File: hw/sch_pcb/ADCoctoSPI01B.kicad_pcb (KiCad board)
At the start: 2 copper layers, 70.6 x 70.6 mm, 79 parts, among them J1 +5V, J10 HEADER_1x02, J11 HEADER_2x04, J2 SATA7-67491-1030, J3 SATA7-67491-1030, J4 SATA7-67491-1030, J5 SATA7-67491-1030, J6 SAS_mini_1888174, J7 SATA7-67491-1030, J8 HEADER_1x02, J9 HEADER_1x02, M1 HOLE, M2 HOLE, M3 HOLE, M4 HOLE, U1 AFE5801, U2 LM1117MP-1,8/NO, U3 LM1117MP-3,3/NO

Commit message: Edit PCB
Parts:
- C10, C11, C12, C13, C14, C15, C16, C17, C18, C19, C2, C20, C21, C22, C23, C24, C25, C26, C27, C28, C29, C3, C33, C34, C35, C36, C37, C38, C39, C4, C5, C6, C7, C8, C9: footprint Mlab_C:SMD-0603_narrow -> Capacitor_SMD:C_0603_1608Metric
- C30, C31: footprint Mlab_R:SMD-0805 -> Capacitor_SMD:C_0805_2012Metric
- R1, R10, R11, R12, R13, R14, R15, R16, R17, R2, R20, R21, R3, R4, R5, R6, R7, R8, R9: footprint Mlab_R:SMD-0603 -> Resistor_SMD:R_0603_1608Metric
- U2, U3: footprint TO_SOT_Packages_SMD:SOT-223-3_TabPin2 -> Package_TO_SOT_SMD:SOT-223-3_TabPin2
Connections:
- J6 pad A10: (no net) -> unconnected-(J6-PadA10)
- J6 pad A11: (no net) -> unconnected-(J6-PadA11)
- J6 pad B10: (no net) -> unconnected-(J6-PadB10)
- J6 pad B11: (no net) -> unconnected-(J6-PadB11)
- J7 pad 5: (no net) -> unconnected-(J7-Pad5)
- J7 pad 6: (no net) -> unconnected-(J7-Pad6)
- U1 pad 26: (no net) -> unconnected-(U1-Pad26)
- U1 pad 27: (no net) -> unconnected-(U1-Pad27)
- U1 pad 60: (no net) -> unconnected-(U1-Pad60)

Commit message: Edit footprints + 3d models
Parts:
- C1: footprint Capacitors_SMD:C_1210_HandSoldering -> Capacitor_SMD:C_1210_3225Metric_Pad1.33x2.70mm_HandSolder
- D1: footprint Diodes_SMD:D_SMA -> Diode_SMD:D_SMA
- L2, L3, L6: footprint Mlab_R:SMD-0805 -> Inductor_SMD:L_0805_2012Metric_Pad1.15x1.40mm_HandSolder
- M1, M2, M3, M4: footprint VIAS:MountingHole_3mm -> Mlab_Mechanical:MountingHole_3mm

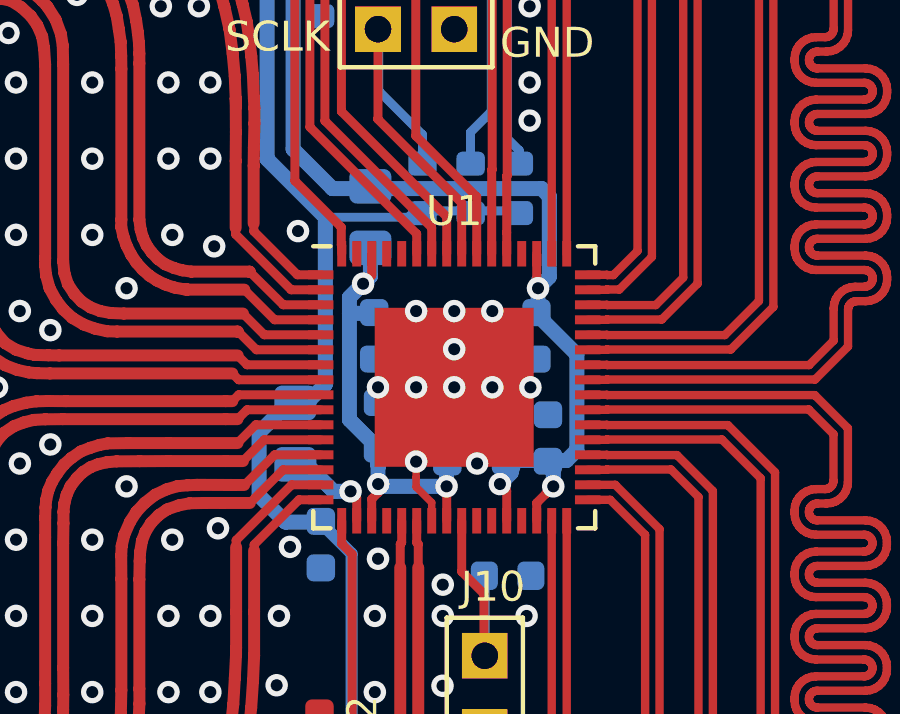
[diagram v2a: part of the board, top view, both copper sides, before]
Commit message: Edit footprint AFE5801
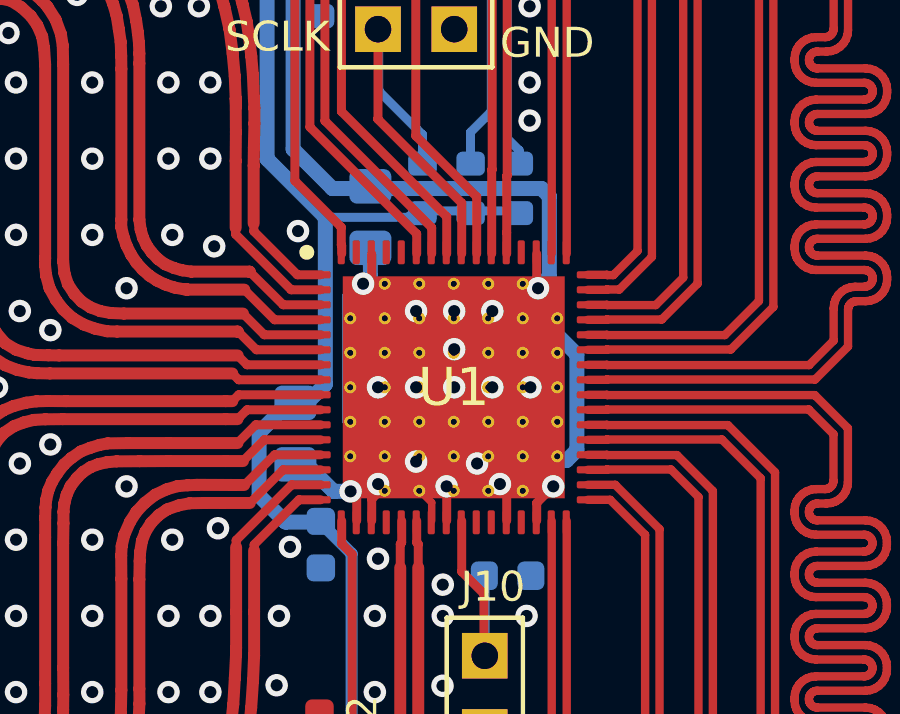
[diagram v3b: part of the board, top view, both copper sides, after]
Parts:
- U1: footprint Mlab_IO:QFN-64-1EP_9x9mm_Pitch0.5mm -> Mlab_IO:VQFN-64_9.15x9.15mm_EP_7.5x7.5mm
- moved U1 3.66 mm to (90.5, 98.7)

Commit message: Edit bom
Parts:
- C1: value 100uF/10V -> 100uF/6V3
- C25: value 100n -> 100nF
- R10, R20: value 127 -> 130
- R11, R21: value 83 -> 82
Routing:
- net GND: track 24.6 -> 104.0 mm, vias 244 -> 251
- net DVDD: track 59.2 -> 0.00 mm, vias 3 -> 0
- net AVDD: track 16.8 -> 0.00 mm, vias 3 -> 0
- net AVDD3V3: track 3.34 -> 0.00 mm, vias 1 -> 0

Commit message: uprava layoutu
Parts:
- moved C20 8.46 mm to (98.4, 100.9), turned to 180 degrees
- moved C21 8.36 mm to (98.4, 99.4), turned to 180 degrees
- moved C19 8.08 mm to (98.4, 97.8), turned to 180 degrees
- moved C36 6.70 mm to (87.4, 100.2), turned to 180 degrees
- moved C39 4.00 mm to (91.2, 110.2), turned to 0 degrees
- moved C35 3.88 mm to (97.5, 105.7), turned to 180 degrees
- moved C34 3.46 mm to (97.5, 102.7), turned to 180 degrees
- moved C33 1.88 mm to (97.5, 104.2), turned to 180 degrees
- moved L3 1.74 mm to (89.7, 94.2), turned to 90 degrees
- moved R14 0.31 mm to (88.4, 88.7)
- moved R13 0.28 mm to (88.4, 85.7)
- moved C27 0.27 mm to (106.3, 69.0)
- moved R15 0.25 mm to (91.4, 95.0)
- moved C31 0.23 mm to (90.3, 74.3)
- moved C28 0.22 mm to (92.2, 74.0)
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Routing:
- net GND: track 104.0 -> 2.94 mm, vias 251 -> 247
- net DVDD: track 0.00 -> 84.6 mm, vias 0 -> 5
- net AVDD: track 0.00 -> 61.2 mm, vias 0 -> 3
- net AVDD3V3: track 0.00 -> 8.15 mm, vias 0 -> 1
- net Net-(C22-Pad2): track 11.5 -> 13.5 mm, vias 0 -> 1
- net Net-(C39-Pad2): track 7.52 -> 6.20 mm
- net Net-(J11-Pad4): track 23.7 -> 24.9 mm
- net VCC: track 25.5 -> 24.6 mm
- net DVDD3V3: track 97.3 -> 96.6 mm
- net unconnected-(J7-Pad6): track 0.56 -> 0.00 mm
- net (no net): vias 1 -> 0

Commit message: uprava layoutu
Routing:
- net GND: track 2.94 -> 9.73 mm
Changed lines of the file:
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@@
   (segment (start 84.82838 116.80952) (end 85.04682 116.32184) (width 0.4) (layer "F.Cu") (net 32))
   (segment (start 79.89316 121.4501) (end 79.89824 121.1707) (width 0.4) (layer "F.Cu") (net 32))
+  (segment (start 90.4448 106.1) (end 90.4448 105.1) (width 0.3) (layer "F.Cu") (net 33))
+  (segment (start 89.4448 97.1) (end 89.4448 97.7448) (width 0.3) (layer "F.Cu") (net 33))
   (segment (start 91.44 104.922002) (end 91.44 104.60732) (width 0.25) (layer "F.Cu") (net 33))
+  (segment (start 90.2 97.9) (end 90.4448 97.6552) (width 0.3) (layer "F.Cu") (net 33))
   (segment (start 112.48028 106.13028) (end 112.522 106.172) (width 0.3) (layer "F.Cu") (net 33))
   (segment (start 114.38028 97.07472) (end 114.427 97.028) (width 0.3) (layer "F.Cu") (net 33))
+  (segment (start 94.9448 106.1) (end 94.9448 105.1) (width 0.3) (layer "F.Cu") (net 33))
+  (segment (start 90.4448 97.6552) (end 90.4448 97.1) (width 0.3) (layer "F.Cu") (net 33))
+  (segment (start 89.6 97.9) (end 90.2 97.9) (width 0.3) (layer "F.Cu") (net 33))
   (segment (start 91.44 104.60732) (end 91.44 104.07699) (width 0.25) (layer "F.Cu") (net 33))
   (segment (start 112.48028 104.51) (end 112.48028 106.13028) (width 0.3) (layer "F.Cu") (net 33))
+  (segment (start 94.9448 97.1) (end 94.9448 98.1) (width 0.2) (layer "F.Cu") (net 33))
+  (segment (start 94.9448 98.1) (end 94.9948 98.15) (width 0.2) (layer "F.Cu") (net 33))
   (segment (start 111.98028 97.06172) (end 112.014 97.028) (width 0.3) (layer "F.Cu") (net 33))
+  (segment (start 94.9448 105.1) (end 94.9948 105.05) (width 0.3) (layer "F.Cu") (net 33))
+  (segment (start 89.4448 97.7448) (end 89.6 97.9) (width 0.3) (layer "F.Cu") (net 33))
+  (segment (start 90.4448 105.1) (end 90.3948 105.05) (width 0.3) (layer "F.Cu") (net 33))
   (segment (start 90.174093 105.110907) (end 90.174093 104.825002) (width 0.3) (layer "F.Cu") (net 33))
+  (segment (start 91.9448 106.1) (end 91.9448 105.45) (width 0.3) (layer "F.Cu") (net 33))
+  (segment (start 91.9448 105.45) (end 91.5448 105.05) (width 0.3) (layer "F.Cu") (net 33))
   (segment (start 123.18028 97.03772) (end 123.19 97.028) (width 0.3) (layer "F.Cu") (net 33))
   (via (at 75.69032 93.977978) (size 0.75) (drill 0.4) (layers "F.Cu" "B.Cu") (net 33))

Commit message: uprava layoutu
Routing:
- net DVDD: track 84.6 -> 87.9 mm
- net DVDD3V3: track 96.6 -> 99.3 mm
- net AVDD3V3: track 8.15 -> 10.3 mm
- net AVDD: track 61.2 -> 62.9 mm
- net GND: vias 247 -> 248

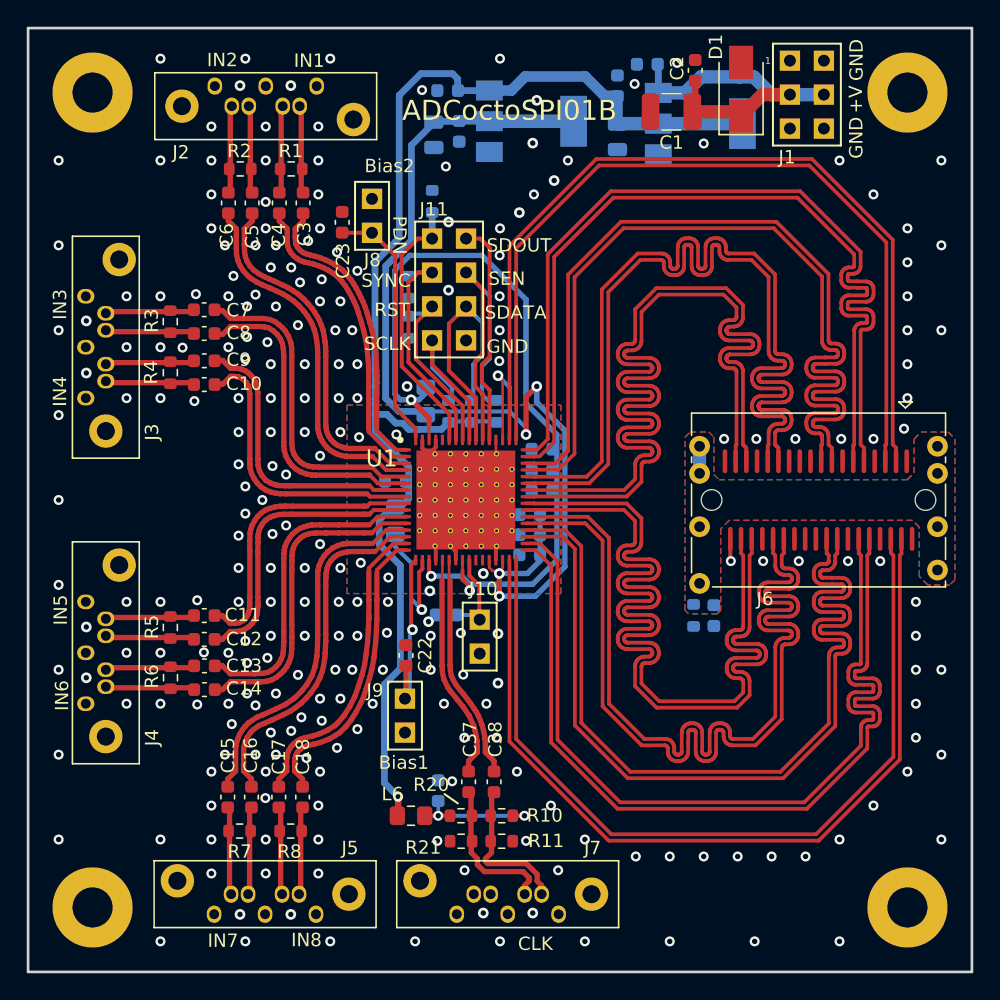
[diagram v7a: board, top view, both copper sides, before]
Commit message: rozdeleni VSSA a VSSD
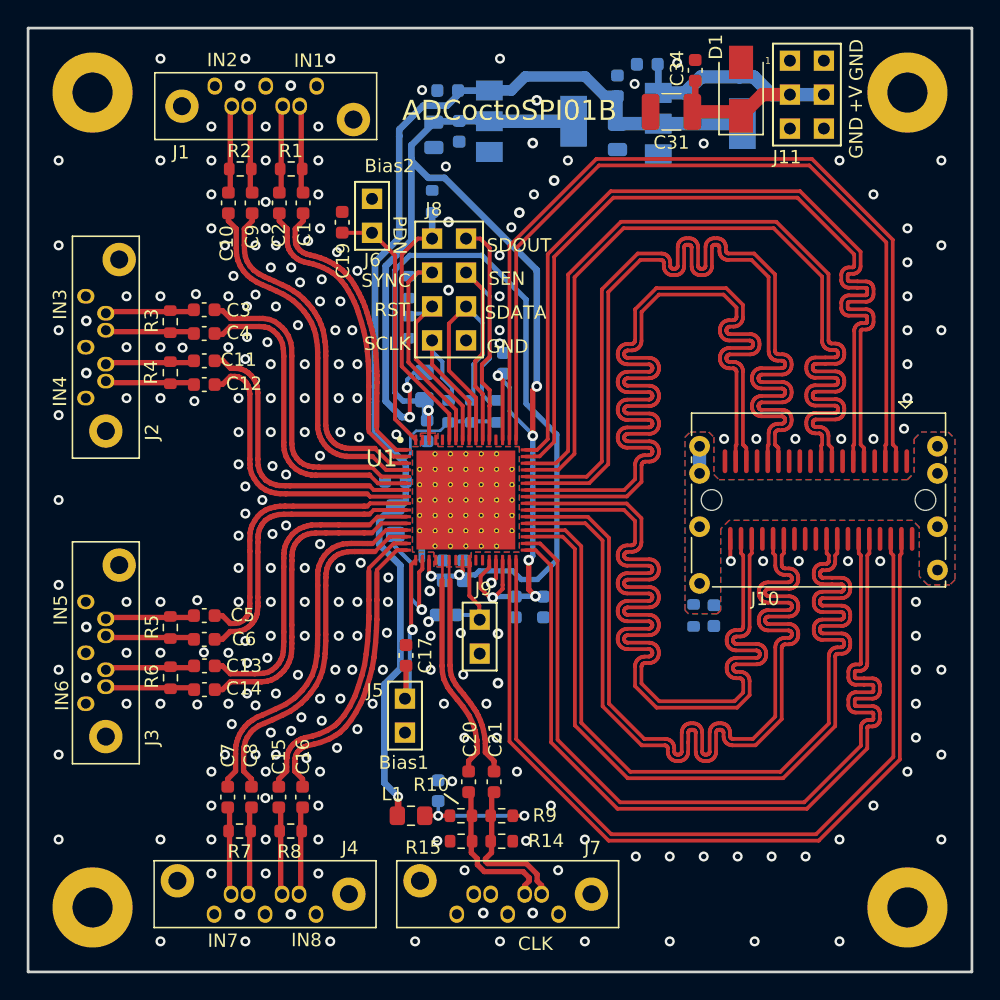
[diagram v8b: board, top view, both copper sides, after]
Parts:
- added JP1: SolderJumper_2_Bridged, NetTie:NetTie-2_SMD_Pad0.5mm, B.Cu at (89.4, 105.6)
- moved C30 11.5 mm to (95.5, 91.4), turned to 90 degrees
- moved C32 9.54 mm to (92.5, 106.9), turned to 90 degrees
- moved C29 9.52 mm to (91.0, 106.9), turned to 90 degrees
- moved C26 8.70 mm to (89.8, 96.4), turned to -90 degrees
- moved C27 5.50 mm to (98.5, 109.6), turned to -90 degrees
- moved C33 4.05 mm to (96.4, 109.6), turned to -90 degrees
- moved L2 1.13 mm to (89.6, 93.1), turned to -90 degrees
- renumbered C3 to C1, C6 to C10, C9 to C11, C10 to C12, C17 to C15, C18 to C16, C22 to C17, C25 to C18, C23 to C19, C4 to C2, C37 to C20, C38 to C21, C39 to C22, C24 to C23, C26 to C24, C27 to C25, C19 to C26, C33 to C27, C36 to C28, C20 to C29, C7 to C3, C34 to C30, C1 to C31, C21 to C32, C35 to C33, C2 to C34, C28 to C35, C29 to C36, C30 to C37, C31 to C38, C8 to C4, C11 to C5, C12 to C6, C15 to C7, C16 to C8, C5 to C9, J2 to J1, J6 to J10, J1 to J11, J3 to J2, J4 to J3, J5 to J4, J9 to J5, J8 to J6, J11 to J8, J10 to J9, L6 to L1, L3 to L2, L2 to L3, R20 to R10, R12 to R11, R13 to R12, R14 to R13, R11 to R14, R21 to R15, R15 to R16, R16 to R17, R17 to R18, R9 to R19, R10 to R9
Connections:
- C26 pad 2: GND -> GNDA
- C29 pad 2: GND -> GNDA
- C32 pad 2: GND -> GNDA
- U1 pad 20: GND -> GNDA
- U1 pad 23: GND -> GNDA
- U1 pad 61: GND -> GNDA
- U1 pad 63: GND -> GNDA
- U1 pad 65: GND -> GNDA
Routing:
- net DVDD: track 87.9 -> 98.1 mm, vias 5 -> 8
- net GND: track 9.73 -> 3.65 mm, vias 248 -> 247
- net DVDD3V3: track 99.3 -> 95.1 mm
- net AVDD: track 62.9 -> 60.7 mm
- net GNDA: track 0.00 -> 1.20 mm
- added copper zone on B.Cu, net GNDA
- added copper zone on F.Cu, net GNDA
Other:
- rule pad_to_mask_clearance: 0.2 -> 0.15
